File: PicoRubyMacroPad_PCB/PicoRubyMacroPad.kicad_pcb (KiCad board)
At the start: 2 copper layers, 99.8 x 91.4 mm, 31 parts, among them SW1 SW_Push, SW10 SW_Push, SW11 SW_Push, SW2 SW_Push, SW3 SW_Push, SW4 SW_Push, SW5 SW_Push, SW6 SW_Push, SW7 SW_Push, SW8 SW_Push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

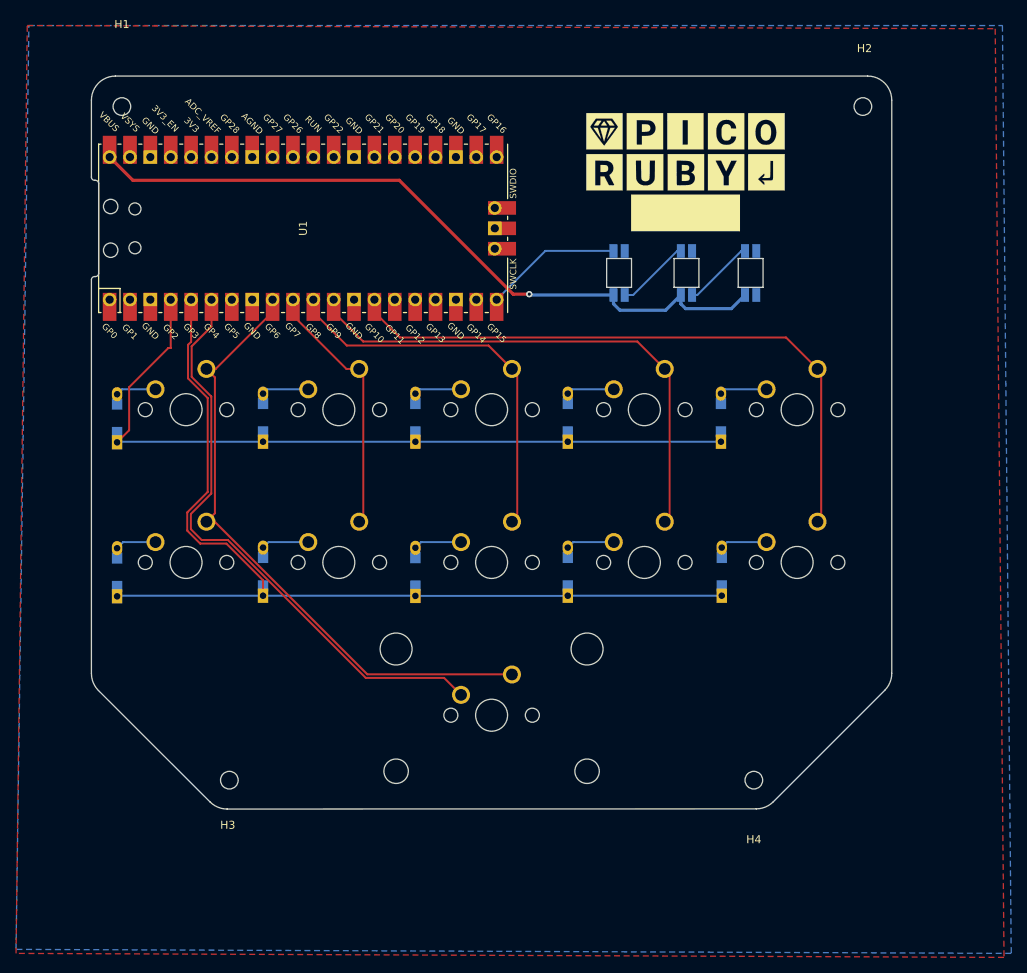
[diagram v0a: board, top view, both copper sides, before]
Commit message: A diode added for SW11
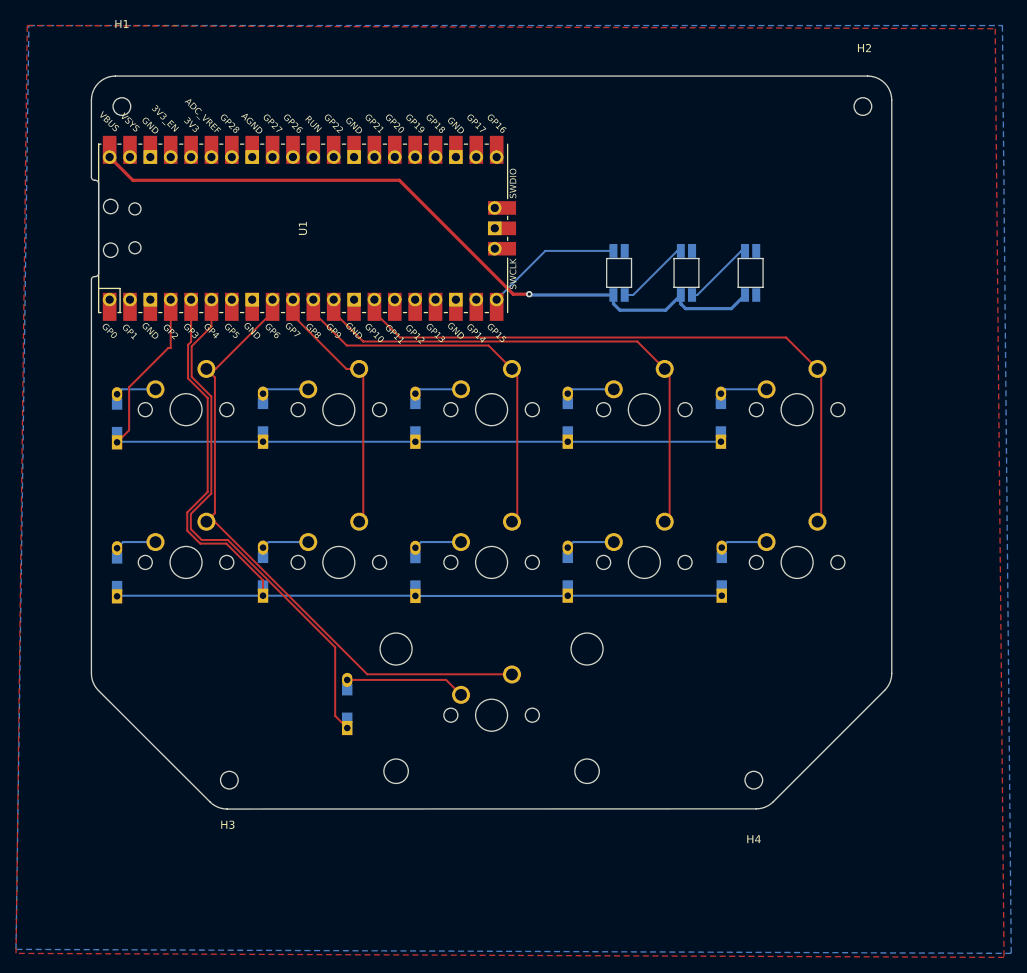
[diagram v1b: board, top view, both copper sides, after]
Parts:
- removed G*** (x2): LOGO, locallib:PicoRuby_Logo
- added D11: D, kbd:D3_TH_SMD_v2, B.Cu at (105.9, 121.7)
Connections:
- SW11 pad 1: R3 -> Net-(D11-Pad2)
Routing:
- net Net-(D11-Pad2): track 0.00 -> 16.2 mm
- net R3: track 74.0 -> 67.7 mm
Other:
- board text added: "PicoRuby & PRK Firmware by hasumikin PCB design by eswai Rev.3 2021.12.05"
- board text removed: "PicoRuby & PRK Firmware by hasumikin PCB design by eswai Rev.2 2021.10.23"
